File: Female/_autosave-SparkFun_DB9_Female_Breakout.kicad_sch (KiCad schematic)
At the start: 12 parts, among them J2 Conn_01x09, J3 DE9-Male

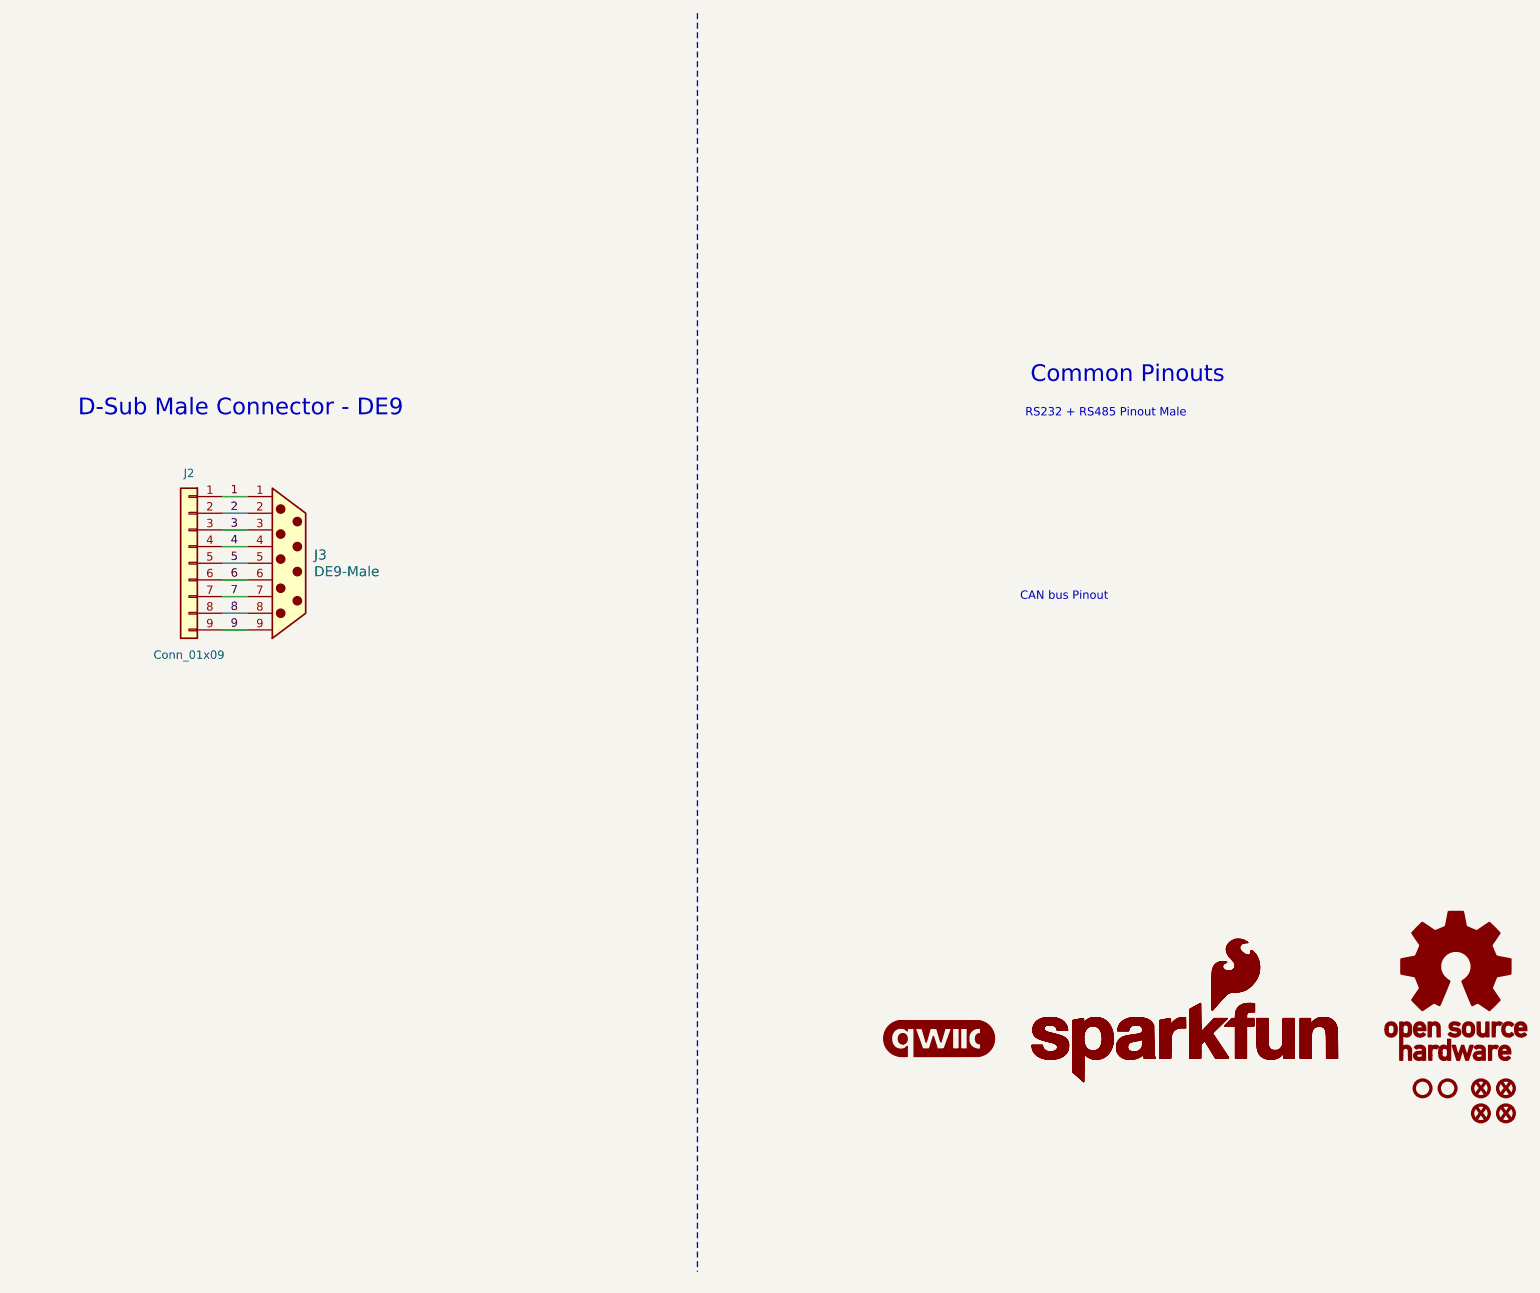
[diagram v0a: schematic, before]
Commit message: Adds a male footprint for the DB9 and updates the affected board
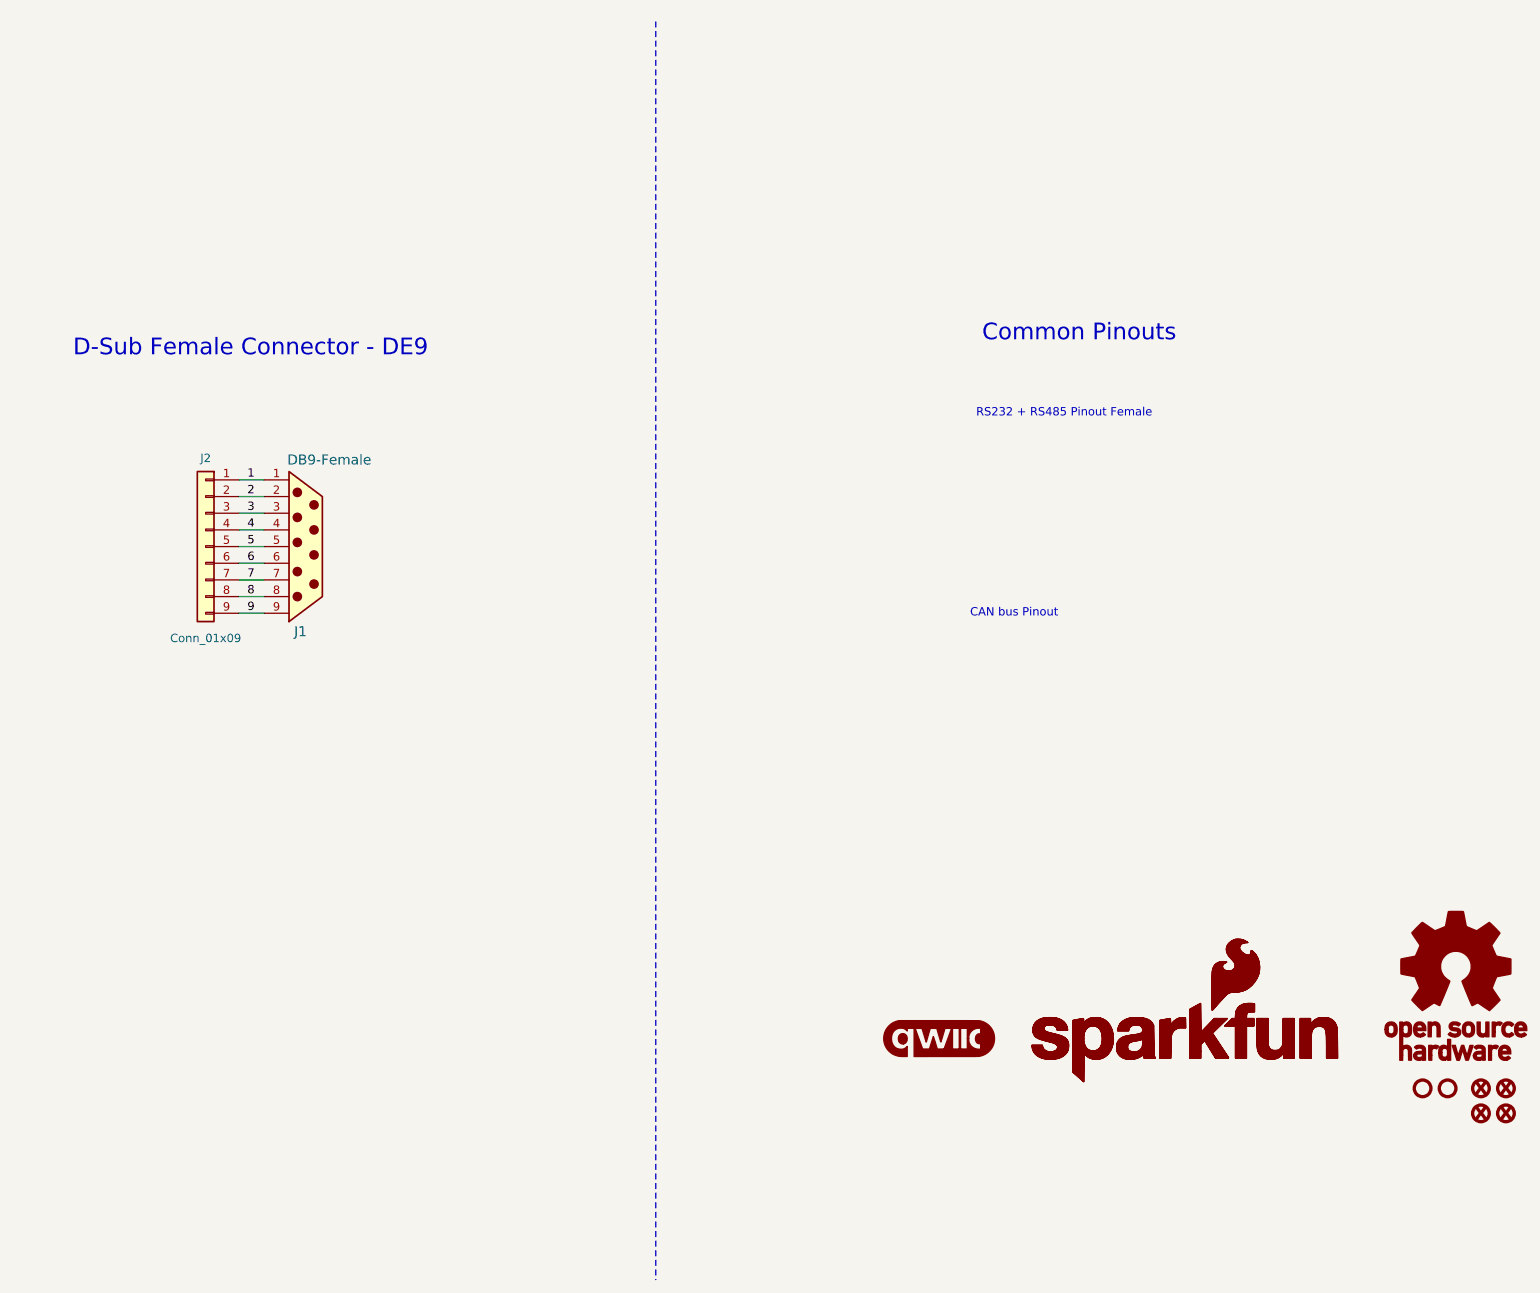
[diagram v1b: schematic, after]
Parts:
- removed J3: DE9-Male, DE9-Footprint:DB9, symbol DB9-Male:DE9-Male
- added J1: DB9-Female, DE9_Footprint:DB9, symbol DB9-Female:DB9 Female
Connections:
- net 1: now also J1.1
- net 2: now also J1.2
- net 3: now also J1.3
- net 4: now also J1.4
- net 5: now also J1.5
- net 6: now also J1.6
- net 7: now also J1.7
- net 8: now also J1.8
- net 9: now also J1.9
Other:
- note added: "D-Sub Female Connector - DE9"
- note added: "RS232 + RS485 Pinout Female"
- note removed: "D-Sub Male Connector - DE9"
- note removed: "RS232 + RS485 Pinout Male"
- moved on the sheet: J2

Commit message: Adds gitignore, Fixes Female DB9 Connector, Adds more silk, Adds GND pins
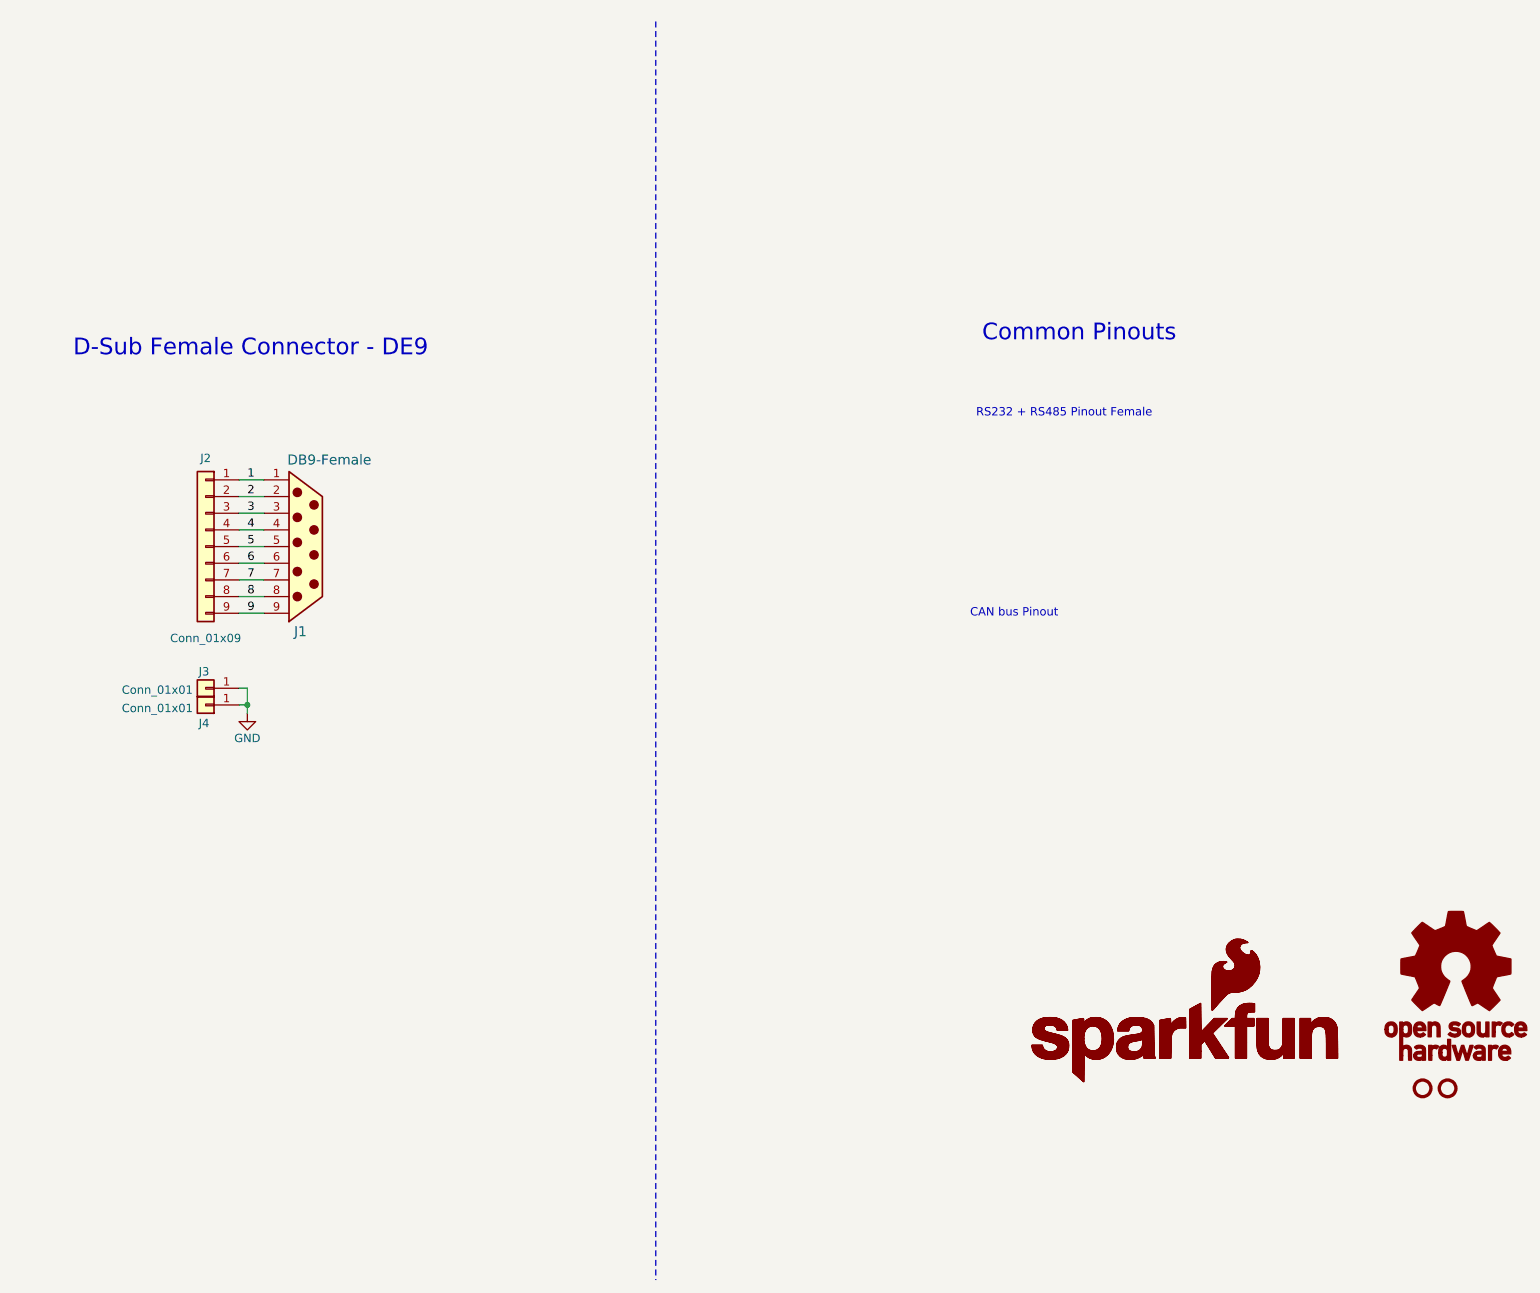
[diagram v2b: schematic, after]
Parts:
- removed FID1, FID2, FID3, FID4: Fiducial_0.5mm, SparkFun-Aesthetic:Fiducial_0.5mm_Mask1mm, symbol SparkFun-Aesthetic:Fiducial_0.5mm
- removed G4: qwiic_Logo, symbol SparkFun-Aesthetic:qwiic_Logo
- added J3, J4: Conn_01x01, SparkFun-Connector:1x01, symbol SparkFun-Connector:Conn_01x01
- J1: footprint DE9_Footprint:DB9 -> DE9_Footprint:DB9_Female
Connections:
- new net GND: J3.1 (Pin_1), J4.1 (Pin_1)
